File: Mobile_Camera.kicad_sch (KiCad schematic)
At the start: 0 parts

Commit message: Change layout
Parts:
- added C1: 1uF, symbol Device:C_Polarized
- added C10, C12: 200nF, symbol Device:C_Small
- added C11, C13, C2, C6, C7, C8, C9: 100nF, symbol Device:C
- added C3, C4: 5pF, symbol Device:C
- added C5: 4.7uF, symbol Device:C_Polarized
- added J1: Conn_01x06, symbol Connector_Generic:Conn_01x06
- added J2: Micro_SD_Card, symbol Connector:Micro_SD_Card
- added J3: Conn_01x24, symbol Connector_Generic:Conn_01x24
- added P1: USB_C_Plug_USB2.0, symbol Connector:USB_C_Plug_USB2.0
- added R1: 10k, symbol Device:R_Small
- added SW1: SW_MEC_5G, symbol Switch:SW_MEC_5G
- added U1: STM32H753VITx, Package_QFP:LQFP-100_14x14mm_P0.5mm, symbol MCU_ST_STM32H7:STM32H753VITx
- added Y1: Crystal, symbol Device:Crystal
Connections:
- new net: C10.2, U1.48 (VCAP1)
- new net: C12.2, U1.73 (VCAP2)
- new net: R1.1, U1.94 (BOOT0)
- new net: P1.A1 (GND), P1.A12 (GND), P1.B1 (GND), P1.B12 (GND)
- new net: P1.A4 (VBUS), P1.A9 (VBUS), P1.B4 (VBUS), P1.B9 (VBUS)
- new net +1V2: J3.10 (Pin_10)
- new net +2V8: J3.11 (Pin_11), J3.4 (Pin_4)
- new net +3V3: C1.1, C11.1, C2.1, C5.1, C6.1, C7.1, C8.1, C9.1, J1.1 (Pin_1), U1.100 (VDD), U1.11 (VDD), U1.21 (VDDA), U1.27 (VDD), U1.50 (VDD), U1.6 (VBAT), U1.75 (VDD)
- new net DCMI_D0: J3.24 (Pin_24), U1.63 (PC6)
- new net DCMI_D1: J3.23 (Pin_23), U1.64 (PC7)
- new net DCMI_D2: J3.19 (Pin_19), U1.97 (PE0)
- new net DCMI_D3: J3.21 (Pin_21), U1.98 (PE1)
- new net DCMI_D4: J3.22 (Pin_22), U1.3 (PE4)
- new net DCMI_D5: J3.20 (Pin_20), U1.84 (PD3)
- new net DCMI_D6: J3.18 (Pin_18), U1.4 (PE5)
- new net DCMI_D7: J3.16 (Pin_16), U1.5 (PE6)
- new net DCMI_HSYNC: J3.9 (Pin_9), U1.28 (PA4)
- new net DCMI_PIXCLK: J3.17 (Pin_17), U1.30 (PA6)
- new net DCMI_VSYNC: J3.7 (Pin_7), U1.93 (PB7)
- new net GND: C1.2, C10.1, C11.2, C12.1, C13.2, C2.2, C3.1, C4.1, C5.2, C6.2, C7.2, C8.2, C9.2, J1.3 (Pin_3), J3.15 (Pin_15), J3.2 (Pin_2), R1.2, SW1.1 (A), SW1.2 (A), U1.10 (VSS), U1.19 (VSSA), U1.26 (VSS), U1.49 (VSS), U1.74 (VSS), U1.99 (VSS)
- new net I2C_SCL: J3.5 (Pin_5), U1.92 (PB6)
- new net I2C_SDA: J3.3 (Pin_3), U1.96 (PB9)
- new net NRST: C13.1, J1.5 (Pin_5), SW1.3 (B), SW1.4 (B), U1.14 (NRST)
- new net PH0: C3.2, U1.12 (PH0), Y1.1
- new net PH1: C4.2, U1.13 (PH1), Y1.2
- new net SWCLK: J1.2 (Pin_2), U1.76 (PA14)
- new net SWDIO: J1.4 (Pin_4), U1.72 (PA13)
- new net SWO: J1.6 (Pin_6), U1.89 (PB3)
- no-connect marks 0 -> 1
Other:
- removed sheet MCU

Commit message: Add SD card and USB C connections
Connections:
- net +3V3 is gone; now on net +5V: C1.1, C11.1, C2.1, C5.1, C6.1, C7.1, C8.1, C9.1, J1.1 (Pin_1), U1.100 (VDD), U1.11 (VDD), U1.21 (VDDA), U1.27 (VDD), U1.50 (VDD), U1.6 (VBAT), U1.75 (VDD)
- net GND: now also J2.6 (VSS), P1.A1 (GND), P1.A12 (GND), P1.B1 (GND), P1.B12 (GND), P1.S1 (SHIELD)
- net I2C_SCL: now also U1.95 (PB8); no longer U1.92 (PB6)
- net SD_DAT0: now reaches U1.65 (PC8)
- net SD_DAT0: now also J2.7 (DAT0)
- net SD_DAT1: now reaches U1.66 (PC9)
- net SD_DAT1: now also J2.8 (DAT1)
- net USB_CC: now reaches U1.69 (PA10)
- net USB_CC: now also P1.A5 (CC)
- net USB_D-: now reaches U1.70 (PA11)
- net USB_D-: now also P1.A7 (D-)
- net USB_D+: now reaches U1.71 (PA12)
- net USB_D+: now also P1.A6 (D+)
- net SD_DAT2: now reaches U1.78 (PC10)
- net SD_DAT2: now also J2.1 (DAT2)
- net SD_DAT3: now reaches U1.79 (PC11)
- net SD_DAT3: now also J2.2 (DAT3/CD)
- net SD_CLK: now reaches U1.80 (PC12)
- net SD_CLK: now also J2.5 (CLK)
- net SD_CMD: now reaches U1.83 (PD2)
- net SD_CMD: now also J2.3 (CMD)
- net +5V: now reaches J2.4 (VDD)
- no-connect marks 1 -> 2
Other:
- moved on the sheet: P1

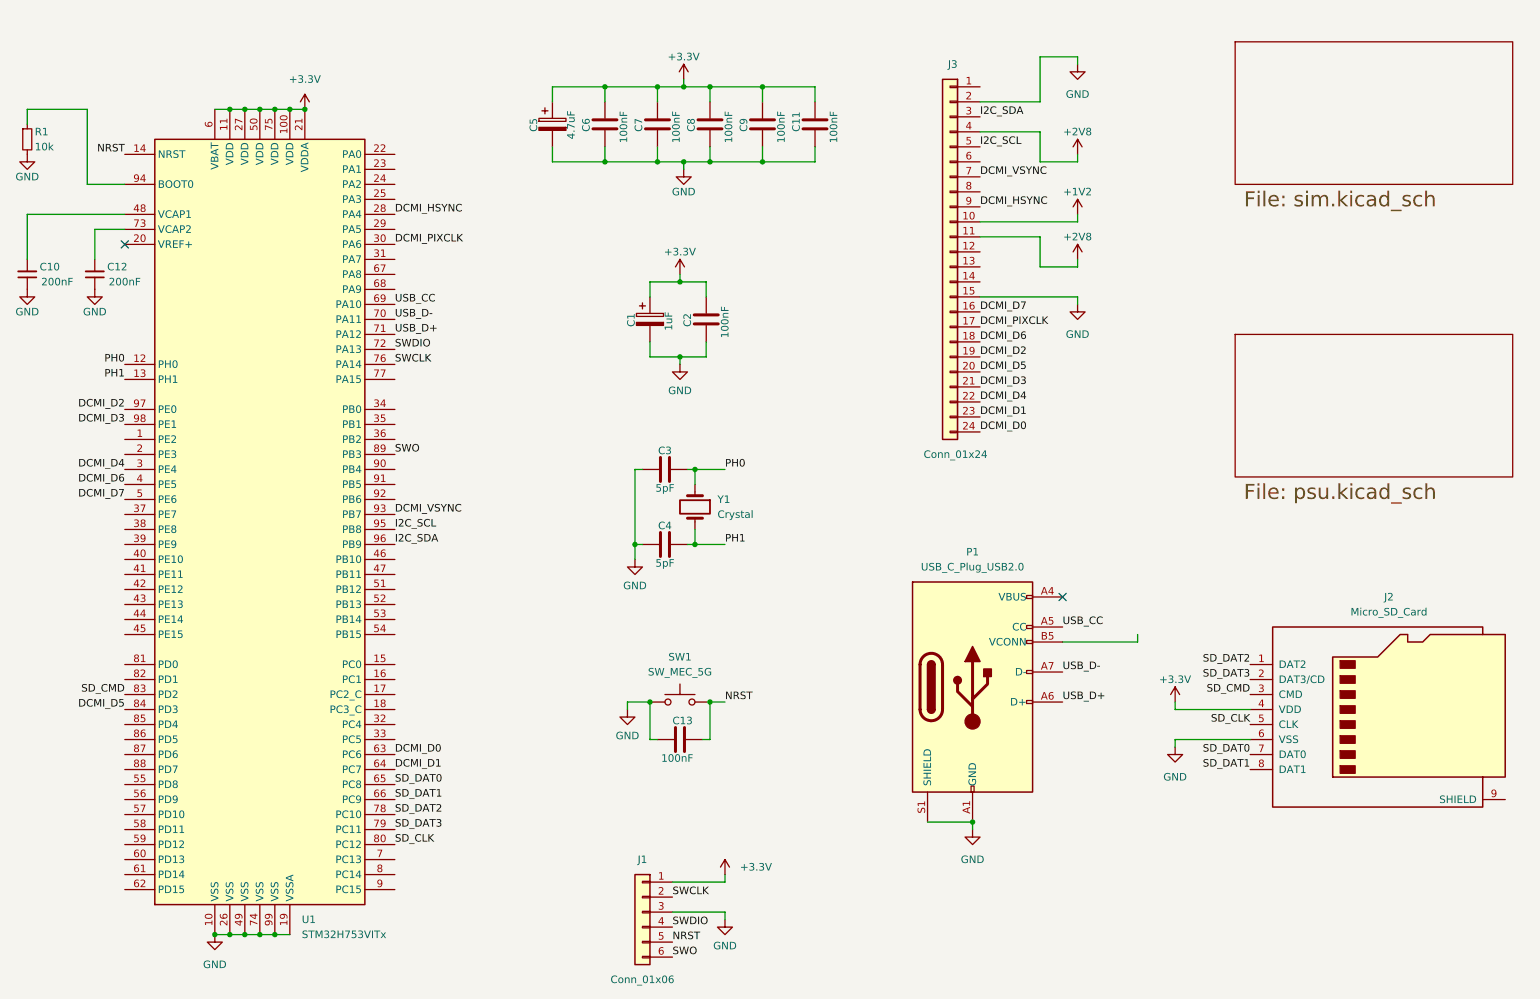
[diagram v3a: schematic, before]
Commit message: Add TSP62851x library and LDO on PSU scheme
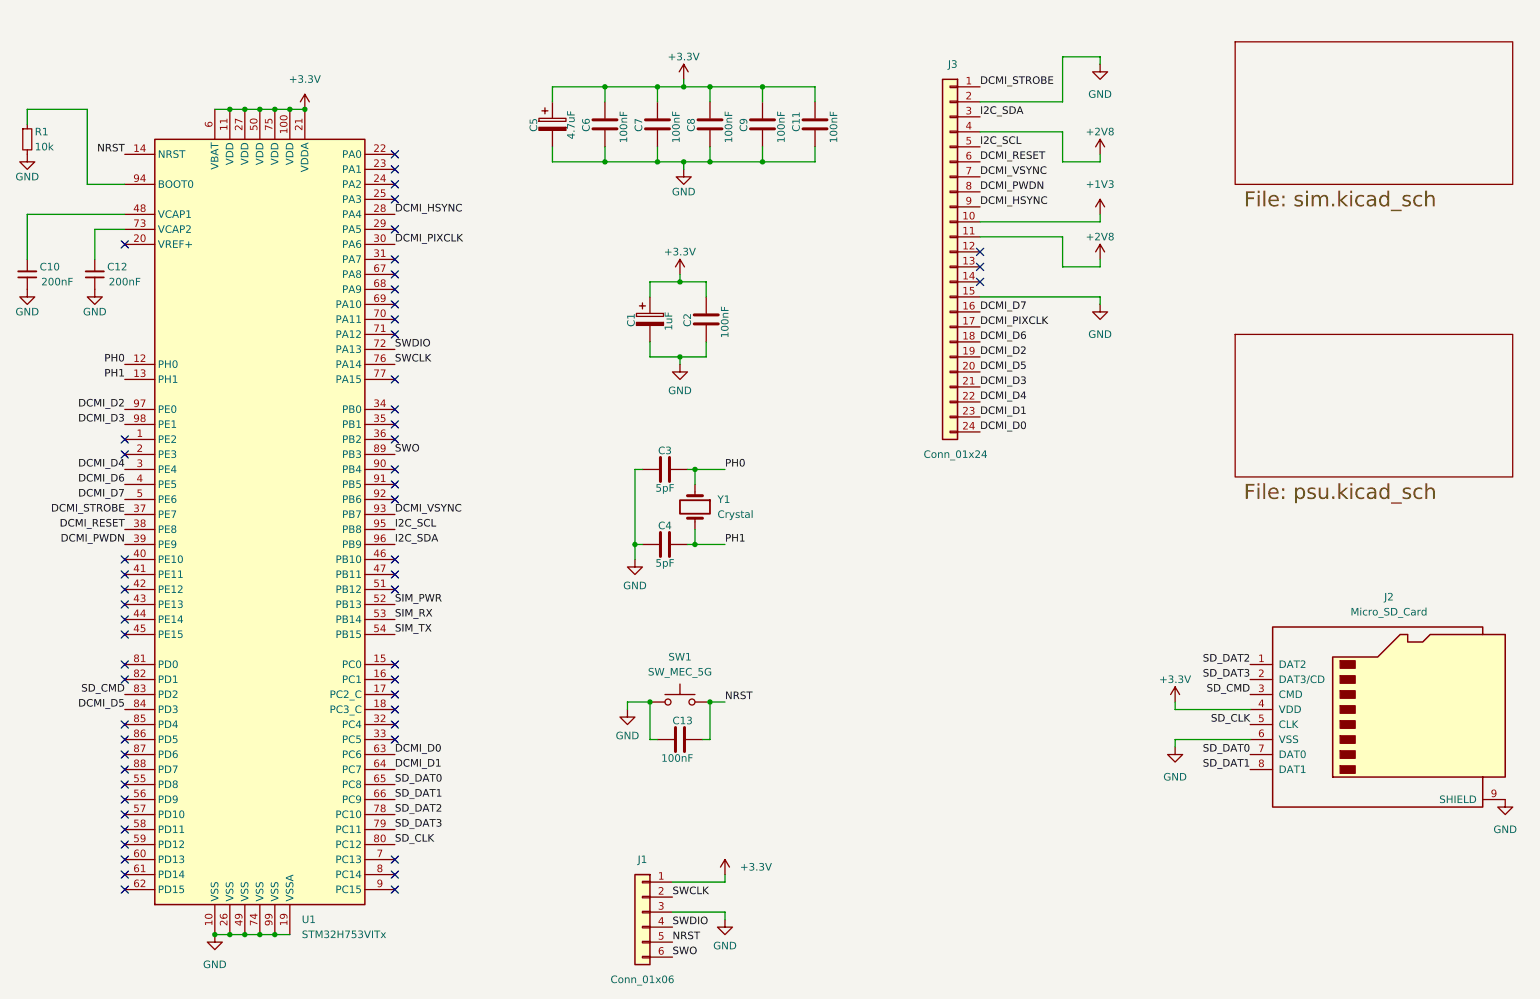
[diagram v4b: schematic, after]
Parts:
- removed P1: USB_C_Plug_USB2.0, symbol Connector:USB_C_Plug_USB2.0
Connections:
- net GND: now also J2.9 (SHIELD)
- net DCMI_STROBE: now reaches U1.37 (PE7)
- net DCMI_STROBE: now also J3.1 (Pin_1)
- net DCMI_RESET: now reaches U1.38 (PE8)
- net DCMI_RESET: now also J3.6 (Pin_6)
- net DCMI_PWDN: now reaches U1.39 (PE9)
- net DCMI_PWDN: now also J3.8 (Pin_8)
- net SIM_PWR: now reaches U1.52 (PB13)
- net SIM_RX: now reaches U1.53 (PB14)
- net SIM_TX: now reaches U1.54 (PB15)
- net +1V2 renamed +1V3
- net USB_CC: no longer names the net of U1.69 (PA10)
- net USB_D+: no longer names the net of U1.71 (PA12)
- net USB_D-: no longer names the net of U1.70 (PA11)
- no-connect marks 2 -> 56

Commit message: Complete schemes, run ERD check tool.
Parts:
- renumbered C10 to C1, C2 to C10, C8 to C11, C9 to C12, C11 to C13, C12 to C2, C5 to C3, C6 to C4, C1 to C5, C7 to C6, C3 to C7, C4 to C8, C13 to C9, J3 to J2, J2 to J3
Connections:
- net +5V renamed +3V3
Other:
- moved on the sheet: J3

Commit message: Assign footprints, change few elements in scheme
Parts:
- added C14: 100nF, Capacitor_SMD:C_0603_1608Metric_Pad1.08x0.95mm_HandSolder, symbol Device:C
- added SW2: Switch_power_on, Button_Switch_SMD:SW_SPST_Omron_B3FS-101xP, symbol Switch:SW_MEC_5G
- C1, C2: value 200nF -> 220nF; footprint (none) -> Capacitor_SMD:C_0603_1608Metric_Pad1.08x0.95mm_HandSolder
- C10, C4: footprint (none) -> Capacitor_SMD:C_0603_1608Metric_Pad1.08x0.95mm_HandSolder
- C11: renamed from C7; footprint (none) -> Capacitor_SMD:C_0603_1608Metric_Pad1.08x0.95mm_HandSolder
- C12: renamed from C8; footprint (none) -> Capacitor_SMD:C_0603_1608Metric_Pad1.08x0.95mm_HandSolder
- C13: renamed from C9; footprint (none) -> Capacitor_SMD:C_0603_1608Metric_Pad1.08x0.95mm_HandSolder
- C3: footprint (none) -> Capacitor_SMD:CP_Elec_4x5.4
- C5: renamed from C6; footprint (none) -> Capacitor_SMD:C_0603_1608Metric_Pad1.08x0.95mm_HandSolder
- C6: renamed from C11; footprint (none) -> Capacitor_SMD:C_0603_1608Metric_Pad1.08x0.95mm_HandSolder
- C7: renamed from C12; footprint (none) -> Capacitor_SMD:C_0603_1608Metric_Pad1.08x0.95mm_HandSolder
- C8: renamed from C13; footprint (none) -> Capacitor_SMD:C_0603_1608Metric_Pad1.08x0.95mm_HandSolder
- C9: renamed from C5; footprint (none) -> Capacitor_SMD:CP_Elec_4x5.4
- J1: value Conn_01x06 -> SWD_header; footprint (none) -> Connector_PinHeader_2.54mm:PinHeader_1x06_P2.54mm_Vertical
- J2: value Conn_01x24 -> DVP_24_pin
- J3: footprint (none) -> Connector_Card:microSD_HC_Wuerth_693072010801
- R1: footprint (none) -> Resistor_SMD:R_0603_1608Metric_Pad0.98x0.95mm_HandSolder
- SW1: value SW_MEC_5G -> Switch_reset; footprint (none) -> Button_Switch_SMD:SW_SPST_Omron_B3FS-101xP
- U1: value STM32H753VITx -> STM32H753VIT6
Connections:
- net GND: now also C14.2, SW2.1 (A), SW2.2 (A)
- net PWR: now reaches U1.22 (PA0)
- net PWR: now also C14.1, SW2.3 (B), SW2.4 (B)
- net +1V3 renamed +1V35
- no-connect marks 56 -> 55
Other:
- moved on the sheet: J3

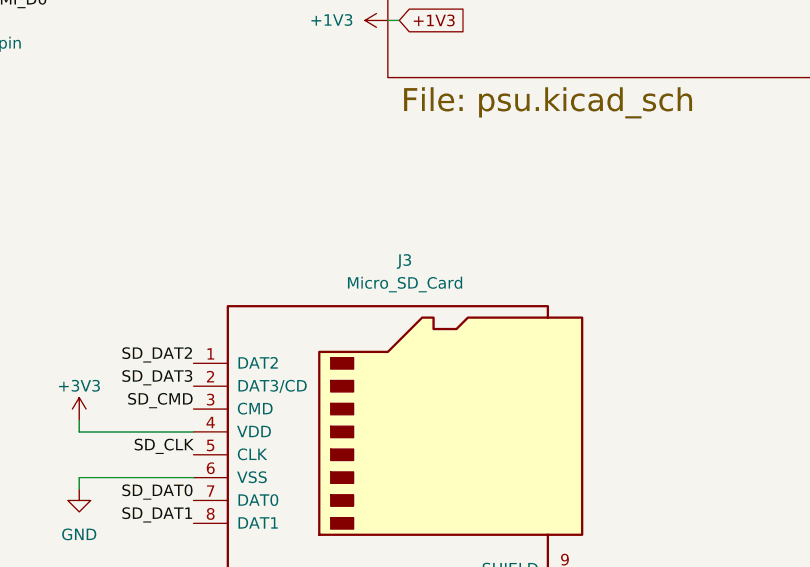
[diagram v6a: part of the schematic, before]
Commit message: Create bill of materials
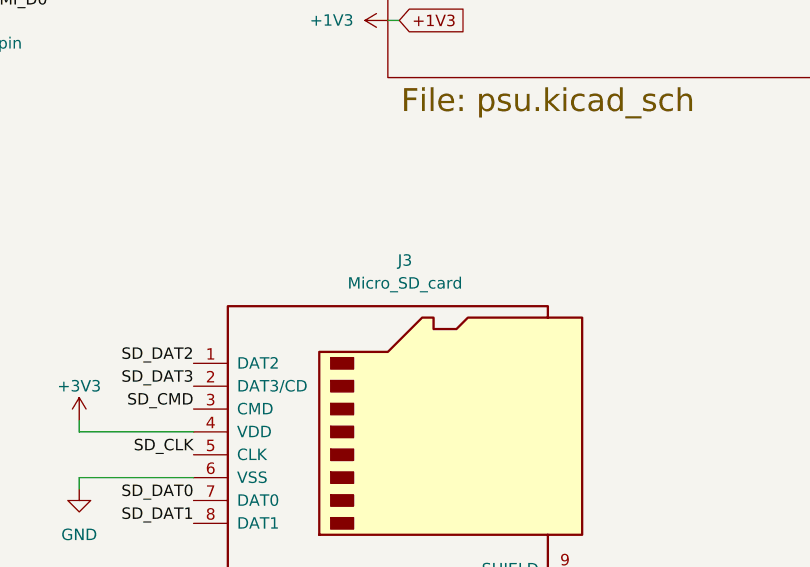
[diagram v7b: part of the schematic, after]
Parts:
- J3: value Micro_SD_Card -> Micro_SD_card
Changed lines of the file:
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@@
       (effects (font (size 1.27 1.27)) hide)
     )
-    (property "Datasheet" "http://www.apem.com/int/index.php?controller=attachment&id_attachment=488" (at 138.43 129.54 0)
+    (property "Datasheet" "~" (at 138.43 129.54 0)
       (effects (font (size 1.27 1.27)) hide)
     )
@@
       (effects (font (size 1.27 1.27)) hide)
     )
-    (property "Datasheet" "http://www.apem.com/int/index.php?controller=attachment&id_attachment=488" (at 172.72 129.54 0)
+    (property "Datasheet" "~" (at 172.72 129.54 0)
       (effects (font (size 1.27 1.27)) hide)
     )
@@
       (effects (font (size 1.27 1.27)))
     )
-    (property "Value" "Micro_SD_Card" (at 236.855 119.38 0)
+    (property "Value" "Micro_SD_card" (at 236.855 119.38 0)
       (effects (font (size 1.27 1.27)))
     )
@@
       (effects (font (size 1.27 1.27)) hide)
     )
-    (property "Datasheet" "http://katalog.we-online.de/em/datasheet/693072010801.pdf" (at 236.22 135.89 0)
-      (effects (font (size 1.27 1.27)) hide)
-    )
+    (property "Datasheet" "~" (at 236.22 135.89 0)
+      (effects (font (size 1.27 1.27)) hide)
+    )

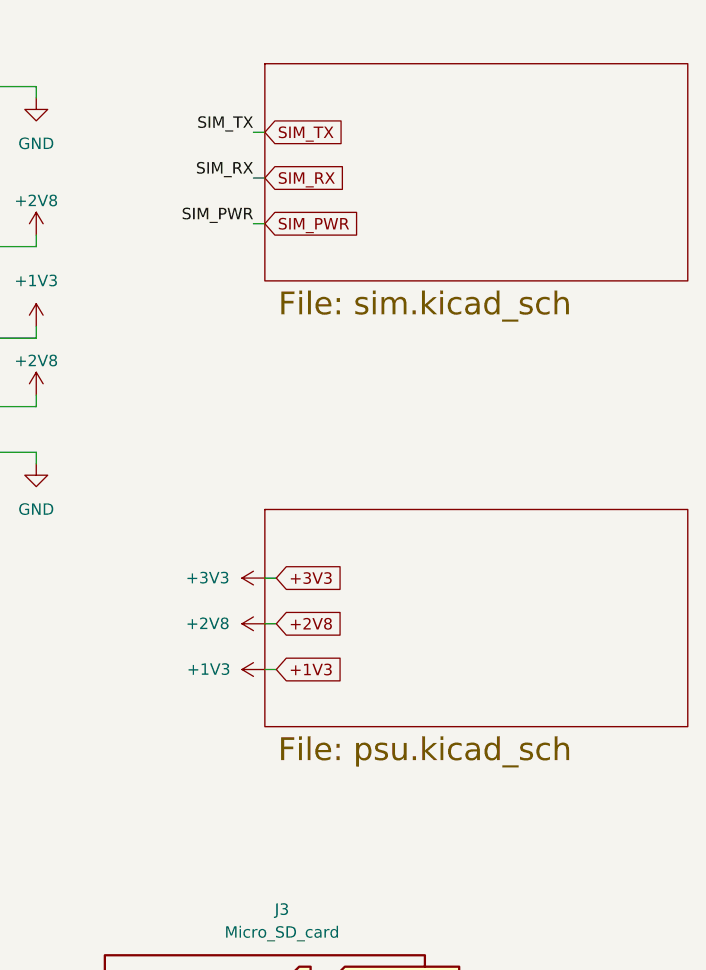
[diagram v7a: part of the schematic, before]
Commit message: Add sub-schemes hierarchical labels
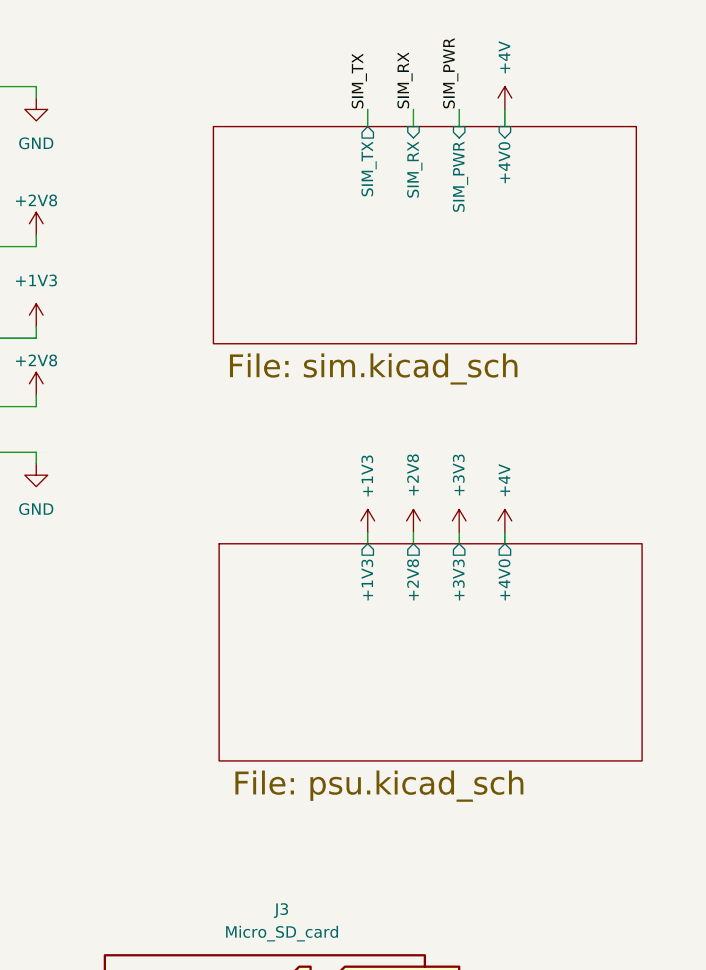
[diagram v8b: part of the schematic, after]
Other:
- sheet PSU ports: added +1V3, +2V8, +3V3, +4V0; removed none
- sheet SIM ports: added +4V0, SIM_PWR, SIM_RX, SIM_TX; removed none
